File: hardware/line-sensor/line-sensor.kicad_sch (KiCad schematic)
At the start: 21 parts, among them J1 Conn_01x07_Socket, Q1 AO3400A, U1 QRE1113GR, U2 QRE1113GR, U3 QRE1113GR, U4 QRE1113GR, U5 QRE1113GR, U6 QRE1113GR

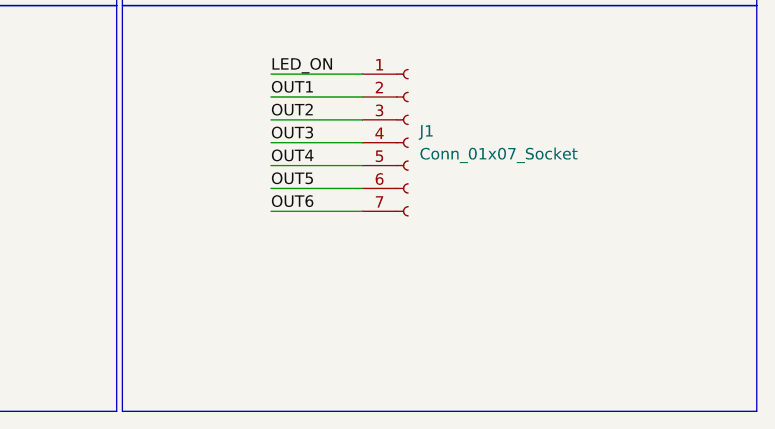
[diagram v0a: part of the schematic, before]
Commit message: added power conn
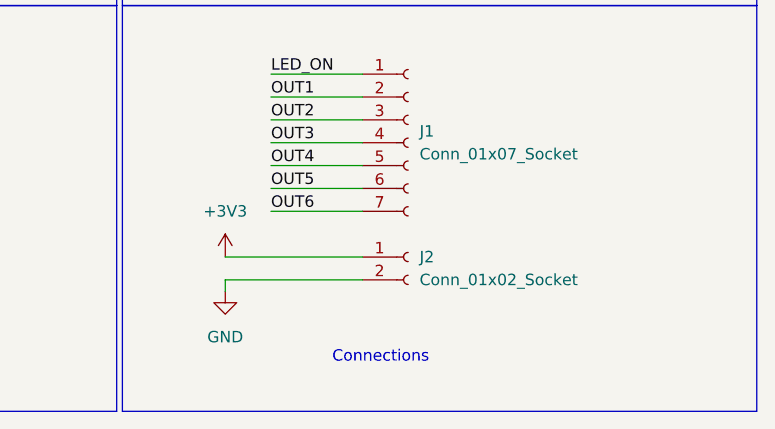
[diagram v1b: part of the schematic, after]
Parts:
- added J2: Conn_01x02_Socket, Connector_PinSocket_1.00mm:PinSocket_1x02_P1.00mm_Vertical_SMD_Pin1Left, symbol Connector:Conn_01x02_Socket
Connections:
- net +3V3: now also J2.1 (Pin_1)
- net GND: now also J2.2 (Pin_2)
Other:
- note added: "Connections"
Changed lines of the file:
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@@
+		)
+	)
+	(text "Connections"
+		(exclude_from_sim no)
+		(at 200.152 112.776 0)
+		(effects
+			(font
+				(size 1.27 1.27)
+			)
 		)
 	)
@@
 	(wire
 		(pts
+			(xy 198.12 104.14) (xy 182.88 104.14)
+		)
+		(stroke
+			(width 0)
+			(type default)
+		)
+	)
+	(wire
+		(pts
 			(xy 154.94 52.07) (xy 162.56 52.07)
 		)
@@
 	(wire
 		(pts
+			(xy 182.88 104.14) (xy 182.88 105.41)
+		)
+		(stroke
+			(width 0)
+			(type default)
+		)
+	)
+	(wire
+		(pts
 			(xy 204.47 57.15) (xy 226.06 57.15)
 		)
@@
 		(pts
 			(xy 118.11 36.83) (xy 111.76 36.83)
+		)
+		(stroke
+			(width 0)
+			(type default)
+		)
+	)
+	(wire
+		(pts
+			(xy 182.88 101.6) (xy 198.12 101.6)
 		)
 		(stroke
@@
 	)
 	(symbol
+		(lib_id "power:GND")
+		(at 182.88 105.41 0)
+		(unit 1)
+		(exclude_from_sim no)
+		(in_bom yes)
+		(on_board yes)
+		(dnp no)
+		(fields_autoplaced yes)
+		(property "Reference" "#PWR021"
+			(at 182.88 111.76 0)
+			(effects
+				(font
+					(size 1.27 1.27)
+				)
+				(hide yes)
+			)
+		)
+		(property "Value" "GND"
+			(at 182.88 110.49 0)
+			(effects
+				(font
+					(size 1.27 1.27)
+				)
+			)
+		)
+		(property "Footprint" ""
+			(at 182.88 105.41 0)
+			(effects
+				(font
+					(size 1.27 1.27)
+				)
+				(hide yes)
+			)
+		)
+		(property "Datasheet" ""
+			(at 182.88 105.41 0)
+			(effects
+				(font
+					(size 1.27 1.27)
+				)
+				(hide yes)
+			)
+		)
+		(property "Description" "Power symbol creates a global label with name \"GND\" , ground"
+			(at 182.88 105.41 0)
+			(effects
+				(font
+					(size 1.27 1.27)
+				)
+				(hide yes)
+			)
+		)
+		(pin "1"
+		)
+		(instances
+			(project ""
+				(path "/be662145-164b-4c7e-b12c-21fb67b1ccf1"
+					(reference "#PWR021")
+					(unit 1)
+				)
+			)
+		)
+	)
+	(symbol
 		(lib_id "power:+3V3")
 		(at 226.06 40.64 0)
@@
 	)
 	(symbol
+		(lib_id "power:+3V3")
+		(at 182.88 101.6 0)
+		(unit 1)
+		(exclude_from_sim no)
+		(in_bom yes)
+		(on_board yes)
+		(dnp no)
+		(fields_autoplaced yes)
+		(property "Reference" "#PWR020"
+			(at 182.88 105.41 0)
+			(effects
+				(font
+					(size 1.27 1.27)
+				)
+				(hide yes)
+			)
+		)
+		(property "Value" "+3V3"
+			(at 182.88 96.52 0)
+			(effects
+				(font
+					(size 1.27 1.27)
+				)
+			)
+		)
+		(property "Footprint" ""
+			(at 182.88 101.6 0)
+			(effects
+				(font
+					(size 1.27 1.27)
+				)
+				(hide yes)
+			)
+		)
+		(property "Datasheet" ""
+			(at 182.88 101.6 0)
+			(effects
+				(font
+					(size 1.27 1.27)
+				)
+				(hide yes)
+			)
+		)
+		(property "Description" "Power symbol creates a global label with name \"+3V3\""
+			(at 182.88 101.6 0)
+			(effects
+				(font
+					(size 1.27 1.27)
+				)
+				(hide yes)
+			)
+		)
+		(pin "1"
+		)
+		(instances
+			(project ""
+				(path "/be662145-164b-4c7e-b12c-21fb67b1ccf1"
+					(reference "#PWR020")
+					(unit 1)
+				)
+			)
+		)
+	)
+	(symbol
 		(lib_id "power:GND")
 		(at 226.06 57.15 0)
@@
 					(unit 1)
 				)
+			)
+		)
+	)
+	(symbol
+		(lib_id "Connector:Conn_01x02_Socket")
+		(at 203.2 101.6 0)
+		(unit 1)
+		(exclude_from_sim no)
+		(in_bom yes)
+		(on_board yes)
+		(dnp no)
+		(fields_autoplaced yes)
+		(property "Reference" "J2"
+			(at 204.47 101.5999 0)
+			(effects
+				(font
+					(size 1.27 1.27)
+				)
+				(justify left)
+			)
+		)
+		(property "Value" "Conn_01x02_Socket"
+			(at 204.47 104.1399 0)
+			(effects
+				(font
+					(size 1.27 1.27)
+				)
+				(justify left)
+			)
+		)
+		(property "Footprint" "Connector_PinSocket_1.00mm:PinSocket_1x02_P1.00mm_Vertical_SMD_Pin1Left"
+			(at 203.2 101.6 0)
+			(effects
+				(font
+					(size 1.27 1.27)
+				)
+				(hide yes)
+			)
+		)
+		(property "Datasheet" "~"
+			(at 203.2 101.6 0)
+			(effects
+				(font
+					(size 1.27 1.27)
+				)
+				(hide yes)
+			)
+		)
+		(property "Description" "Generic connector, single row, 01x02, script generated"
+			(at 203.2 101.6 0)
+			(effects
+				(font
+					(size 1.27 1.27)
+				)
+				(hide yes)
+			)
+		)
+		(pin "2"
+		)
+		(pin "1"
+		)
+		(instances
+			(project ""
+				(path "/be662145-164b-4c7e-b12c-21fb67b1ccf1"
+					(reference "J2")
+					(unit 1)
+				)

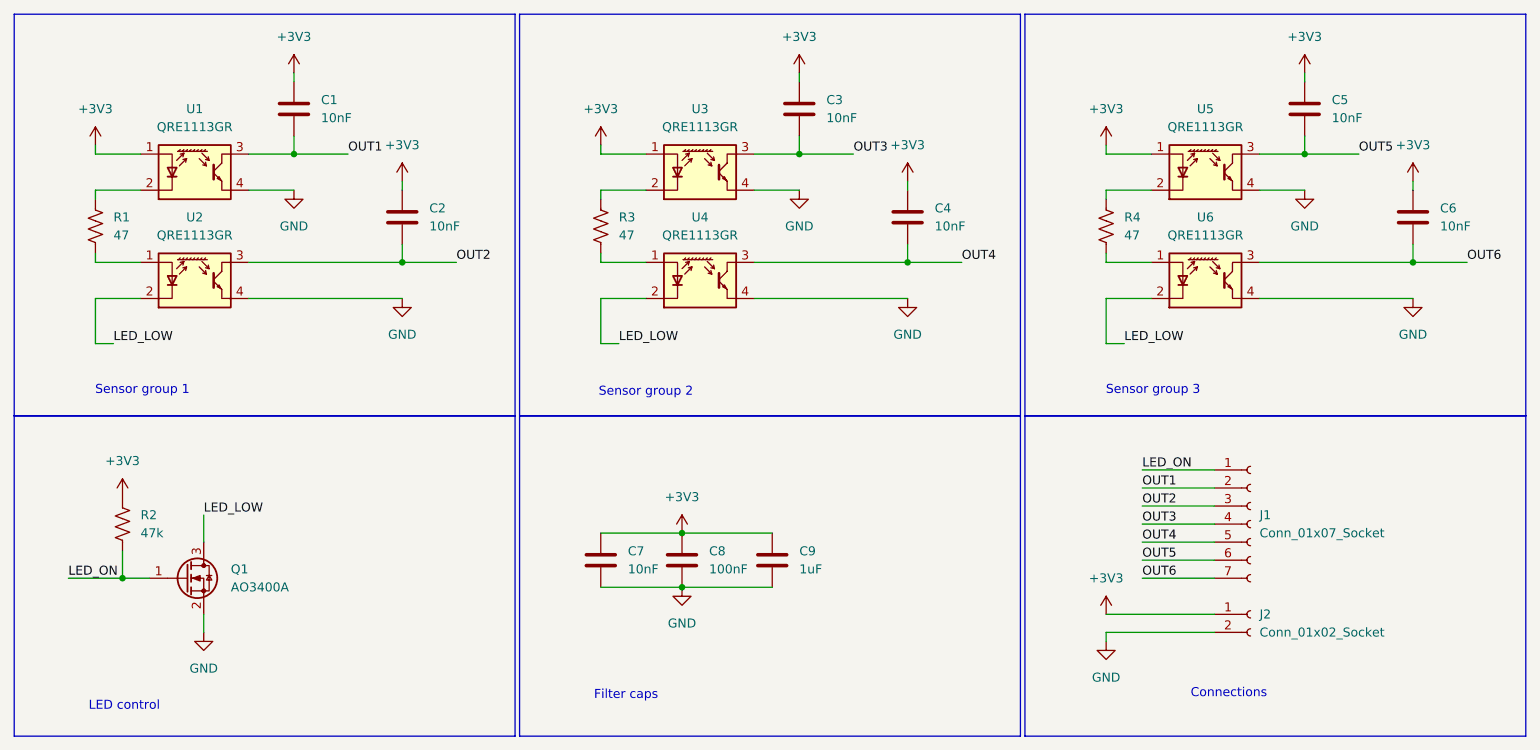
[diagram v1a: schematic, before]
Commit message: added LCSC part number to schematic
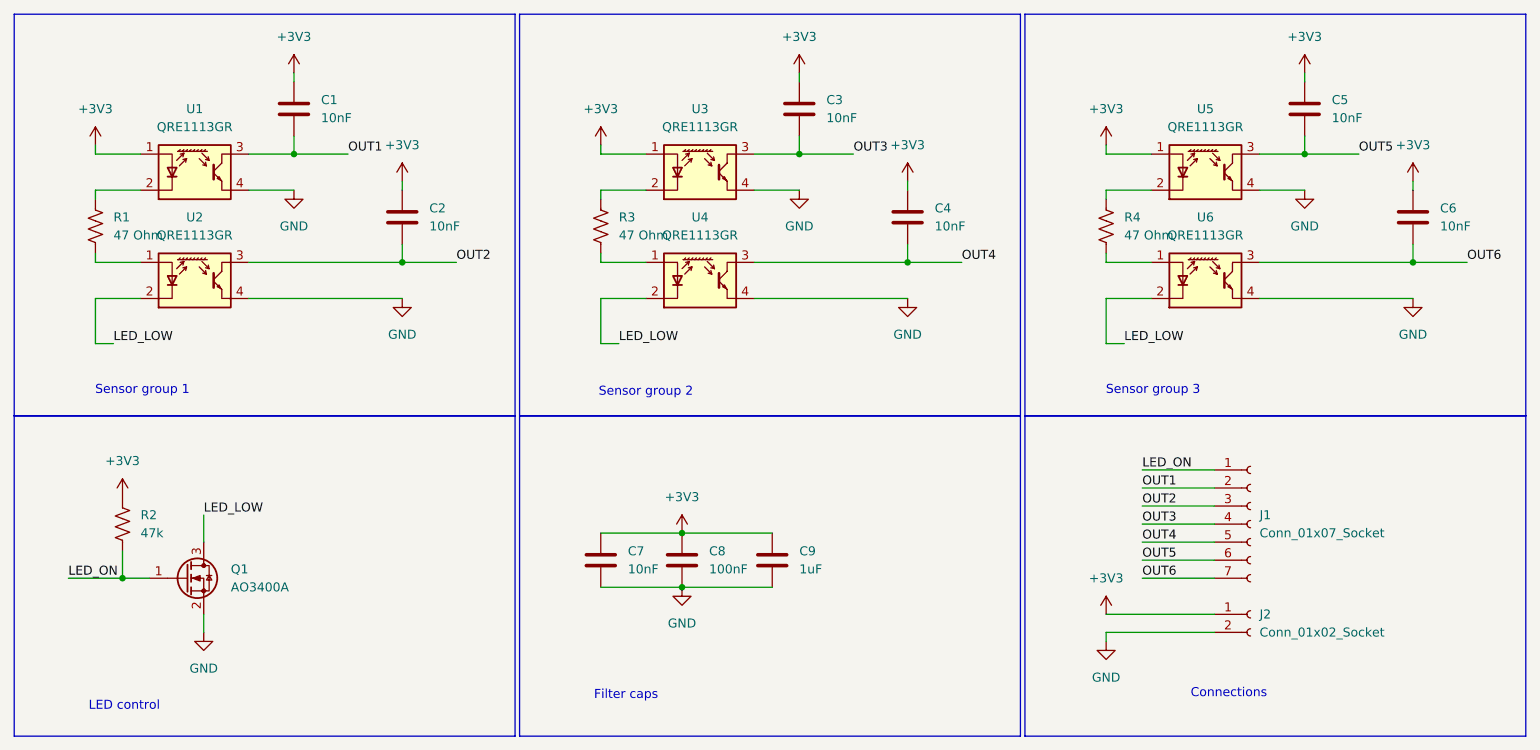
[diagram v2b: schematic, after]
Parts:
- J1: LCSC (none) -> C42379199
- J2: LCSC (none) -> C42381025
- Q1: LCSC (none) -> C20917
- R1, R3, R4: value 47 -> 47 Ohm
- U1, U2, U3, U4, U5, U6: LCSC (none) -> C232862
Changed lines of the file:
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@@
+			)
+		)
+		(property "LCSC" "C232862"
+			(at 125.73 39.37 0)
+			(effects
+				(font
+					(size 1.27 1.27)
+				)
+				(hide yes)
 			)
 		)
@@
 			)
 		)
+		(property "LCSC" "C232862"
+			(at 196.85 39.37 0)
+			(effects
+				(font
+					(size 1.27 1.27)
+				)
+				(hide yes)
+			)
+		)
 		(pin "4"
 		)
@@
 			)
 		)
-		(property "Value" "47"
+		(property "Value" "47 Ohm"
 			(at 43.18 48.2599 0)
 			(effects
@@
 			)
 		)
-		(property "Value" "47"
+		(property "Value" "47 Ohm"
 			(at 114.3 48.2599 0)
 			(effects
@@
 			)
 		)
+		(property "LCSC" "C42379199"
+			(at 203.2 88.9 0)
+			(effects
+				(font
+					(size 1.27 1.27)
+				)
+				(hide yes)
+			)
+		)
 		(pin "7"
 		)
@@
 			)
 		)
+		(property "LCSC" "C232862"
+			(at 54.61 54.61 0)
+			(effects
+				(font
+					(size 1.27 1.27)
+				)
+				(hide yes)
+			)
+		)
 		(pin "4"
 		)
@@
 			)
 		)
+		(property "LCSC" "C232862"
+			(at 125.73 54.61 0)
+			(effects
+				(font
+					(size 1.27 1.27)
+				)
+				(hide yes)
+			)
+		)
 		(pin "4"
 		)
@@
 			)
 		)
+		(property "LCSC" "C232862"
+			(at 196.85 54.61 0)
+			(effects
+				(font
+					(size 1.27 1.27)
+				)
+				(hide yes)
+			)
+		)
 		(pin "4"
 		)
@@
 			)
 		)
+		(property "LCSC" "C42381025"
+			(at 203.2 101.6 0)
+			(effects
+				(font
+					(size 1.27 1.27)
+				)
+				(hide yes)
+			)
+		)
 		(pin "2"
 		)
@@
 			)
 		)
-		(property "Value" "47"
+		(property "Value" "47 Ohm"
 			(at 185.42 48.2599 0)
 			(effects
@@
 			)
 		)
+		(property "LCSC" "C20917"
+			(at 53.34 96.52 0)
+			(effects
+				(font
+					(size 1.27 1.27)
+				)
+				(hide yes)
+			)
+		)
 		(pin "3"
 		)
@@
 			(at 54.61 39.37 0)
 			(effects
+				(font
+					(size 1.27 1.27)
+				)
+				(hide yes)
+			)
+		)
+		(property "LCSC" "C232862"
+			(at 54.61 39.37 0)
+			(effects

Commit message: Not sure why this wasn't committed
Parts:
- added R10, R5, R6, R7, R8, R9: 220, Resistor_SMD:R_0603_1608Metric_Pad0.98x0.95mm_HandSolder, symbol Device:R_US
- C1, C2, C3, C4, C5, C6, C7, C8, C9: footprint (none) -> Capacitor_SMD:C_0603_1608Metric_Pad1.08x0.95mm_HandSolder
- J2: footprint Connector_PinSocket_1.00mm:PinSocket_1x02_P1.00mm_Vertical_SMD_Pin1Left -> Connector_PinSocket_2.54mm:PinSocket_1x02_P2.54mm_Vertical_SMD_Pin1Right
- R1, R2, R3, R4: footprint (none) -> Resistor_SMD:R_0603_1608Metric_Pad0.98x0.95mm_HandSolder
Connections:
- net OUT1: now also R5.2; no longer C1.2, U1.3
- net OUT2: now also R6.2; no longer C2.2, U2.3
- net OUT3: now also R7.2; no longer C3.2, U3.3
- net OUT4: now also R8.2; no longer C4.2, U4.3
- net OUT5: now also R9.2; no longer C5.2, U5.3
- net OUT6: now also R10.2; no longer C6.2, U6.3
- new net: C3.2, R7.1, U3.3
- new net: C5.2, R9.1, U5.3
- new net: C4.2, R8.1, U4.3
- new net: C2.2, R6.1, U2.3
- new net: C6.2, R10.1, U6.3
- new net: C1.2, R5.1, U1.3
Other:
- moved on the sheet: C1
